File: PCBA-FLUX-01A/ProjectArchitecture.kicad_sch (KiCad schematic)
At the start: 0 parts

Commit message: Changes were made
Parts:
- added J1, J2, J3: Conn_02x06_Odd_Even, Connector_PinHeader_2.54mm:PinHeader_2x06_P2.54mm_Vertical, symbol Connector_Generic:Conn_02x06_Odd_Even
- added J4, J5, J6: Screw_Terminal_01x01, symbol Connector:Screw_Terminal_01x01
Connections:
- new net GND: J1.10 (Pin_10), J1.11 (Pin_11), J1.2 (Pin_2), J1.3 (Pin_3), J1.6 (Pin_6), J1.7 (Pin_7), J2.10 (Pin_10), J2.11 (Pin_11), J2.2 (Pin_2), J2.3 (Pin_3), J2.6 (Pin_6), J2.7 (Pin_7), J3.10 (Pin_10), J3.11 (Pin_11), J3.2 (Pin_2), J3.3 (Pin_3), J3.6 (Pin_6), J3.7 (Pin_7)
- new net Phase U/PhaseU_out: J4.1 (Pin_1)
- new net Phase U/phU_HI: J1.1 (Pin_1)
- new net Phase U/phU_LO: J1.5 (Pin_5)
- new net Phase U/phU_NTCctrl: J1.4 (Pin_4)
- new net Phase U/phU_NTCout: J1.8 (Pin_8)
- new net Phase U/phU_current: J1.9 (Pin_9)
- new net Phase U/phU_voltage: J1.12 (Pin_12)
- new net Phase V/PhaseV_out: J5.1 (Pin_1)
- new net Phase V/phV_HI: J2.1 (Pin_1)
- new net Phase V/phV_LO: J2.5 (Pin_5)
- new net Phase V/phV_NTCctrl: J2.8 (Pin_8)
- new net Phase V/phV_NTCout: J2.4 (Pin_4)
- new net Phase V/phV_current: J2.9 (Pin_9)
- new net Phase V/phV_voltage: J2.12 (Pin_12)
- new net Phase W/PhaseW_out: J6.1 (Pin_1)
- new net Phase W/phW_HI: J3.1 (Pin_1)
- new net Phase W/phW_LO: J3.5 (Pin_5)
- new net Phase W/phW_NTCctrl: J3.8 (Pin_8)
- new net Phase W/phW_NTCout: J3.4 (Pin_4)
- new net Phase W/phW_current: J3.9 (Pin_9)
- new net Phase W/phW_voltage: J3.12 (Pin_12)
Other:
- sheet Phase U ports: added PhaseU_out, phU_HI, phU_LO, phU_NTCctrl, phU_NTCout, phU_current, phU_voltage; removed none
- sheet Phase V ports: added PhaseV_out, phV_HI, phV_LO, phV_NTCctrl, phV_NTCout, phV_current, phV_voltage; removed none
- sheet Phase W ports: added PhaseW_out, phW_HI, phW_LO, phW_NTCctrl, phW_NTCout, phW_current, phW_voltage; removed none

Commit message: Finished schematic?
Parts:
- added J10, J9: Screw_Terminal_01x01, Bvrny's_library:M8_NutTerminal, symbol Connector:Screw_Terminal_01x01
- added J7, J8: Conn_02x02_Odd_Even, Connector_PinHeader_2.54mm:PinHeader_2x02_P2.54mm_Vertical, symbol Connector_Generic:Conn_02x02_Odd_Even
- J4, J5, J6: footprint (none) -> Bvrny's_library:M8_NutTerminal; now not fitted
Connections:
- net GND: now also J10.1 (Pin_1), J8.1 (Pin_1), J8.2 (Pin_2), J8.3 (Pin_3), J8.4 (Pin_4)
- new net +VSYS: J7.1 (Pin_1), J7.2 (Pin_2), J7.3 (Pin_3), J7.4 (Pin_4), J9.1 (Pin_1)
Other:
- removed sheet Power Input
- note added: "Board connectors for power to Vector"
- note added: "Board connectors to Vector"
- note added: "High current connectors"
- note added: "Inverter"
- note added: "Power input connectors"
- moved on the sheet: J1, J2, J3

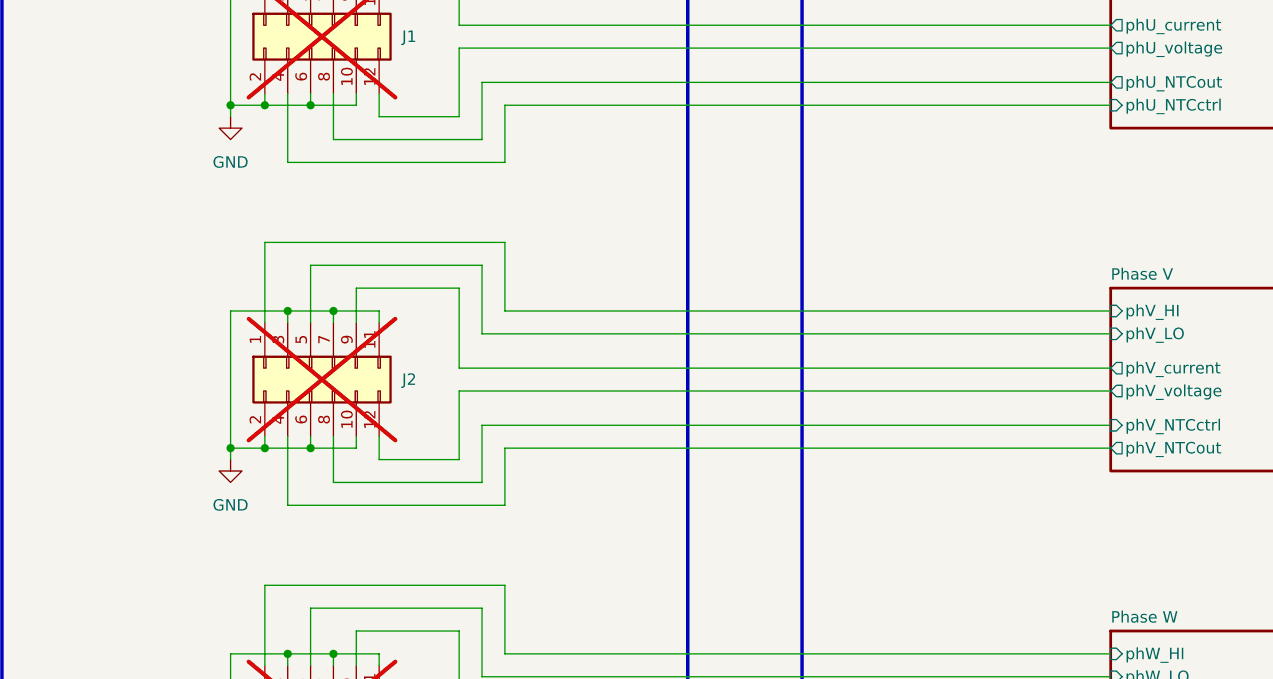
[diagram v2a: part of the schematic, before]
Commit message: Started with Flux layout
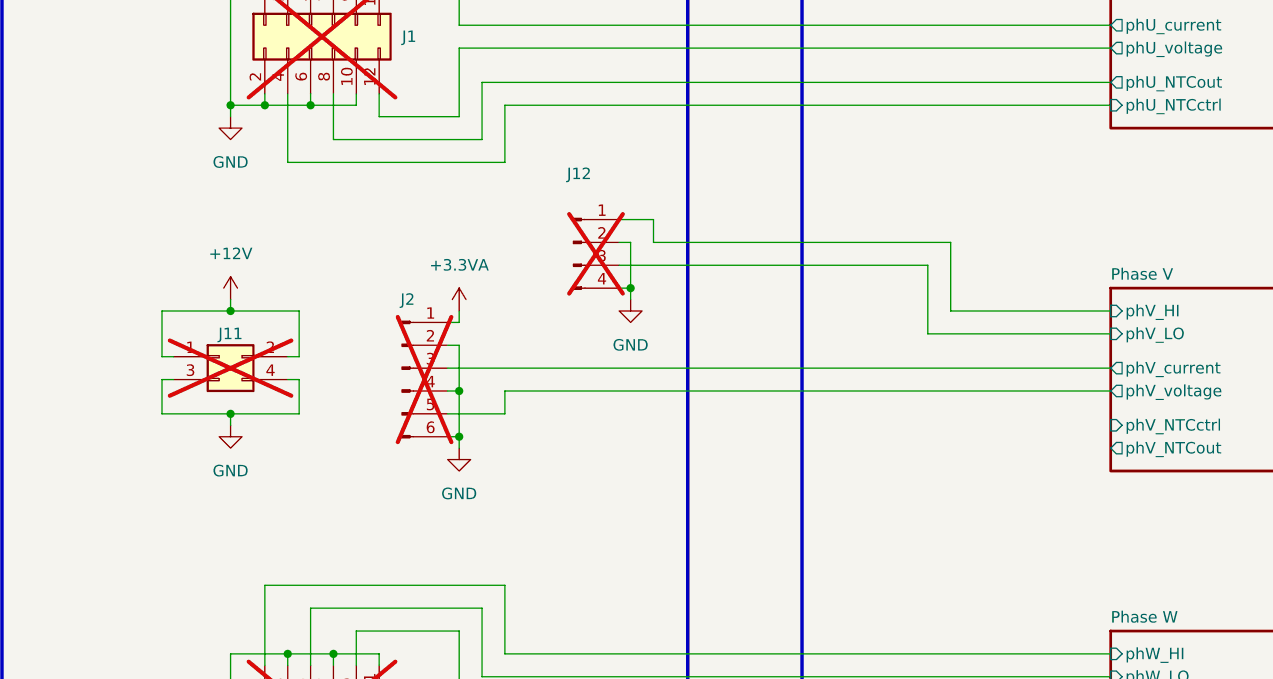
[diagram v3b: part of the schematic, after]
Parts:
- removed J2: Conn_02x06_Odd_Even, Connector_PinHeader_2.54mm:PinHeader_2x06_P2.54mm_Vertical, symbol Connector_Generic:Conn_02x06_Odd_Even
- added J11: Conn_02x02_Odd_Even, Connector_PinHeader_2.54mm:PinHeader_2x02_P2.54mm_Vertical, symbol Connector_Generic:Conn_02x02_Odd_Even
- added J12: Conn_01x04_Pin, Connector_PinHeader_2.54mm:PinHeader_1x04_P2.54mm_Vertical, symbol Connector:Conn_01x04_Pin
- added J2: Conn_01x06_Pin, Connector_PinHeader_2.54mm:PinHeader_1x06_P2.54mm_Vertical, symbol Connector:Conn_01x06_Pin
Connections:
- net GND: now also J11.3 (Pin_3), J11.4 (Pin_4), J12.2 (Pin_2), J12.4 (Pin_4), J2.2 (Pin_2), J2.4 (Pin_4), J2.6 (Pin_6)
- net Phase V/phV_HI: now also J12.1 (Pin_1)
- net Phase V/phV_LO: now also J12.3 (Pin_3)
- net Phase V/phV_current: now also J2.3 (Pin_3)
- net Phase V/phV_voltage: now also J2.5 (Pin_5)
- new net +12V: J11.1 (Pin_1), J11.2 (Pin_2)
- new net +3.3VA: J2.1 (Pin_1)

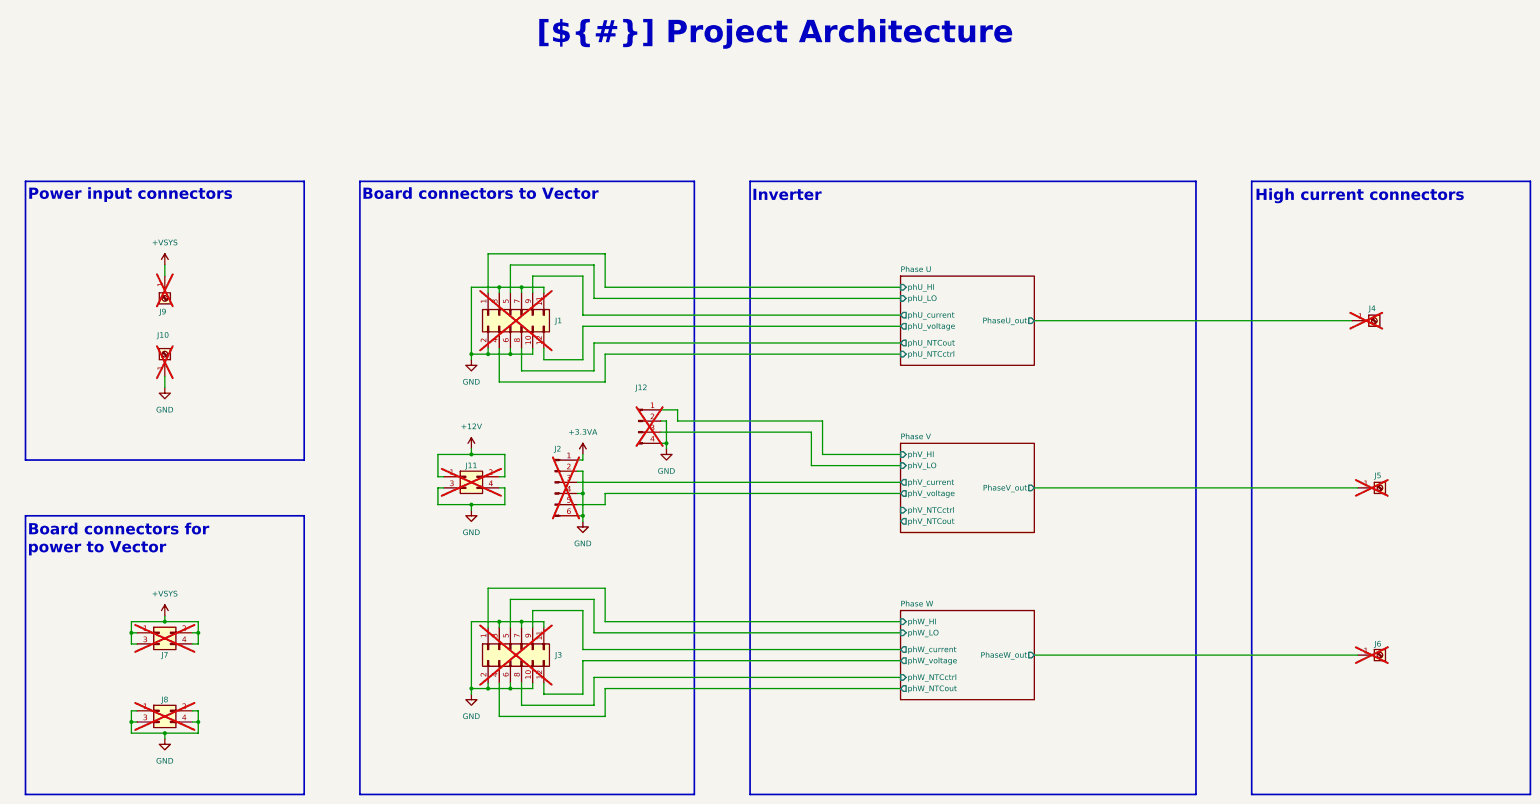
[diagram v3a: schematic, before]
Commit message: Moved the current and voltage sensing OpAmp's to Vector
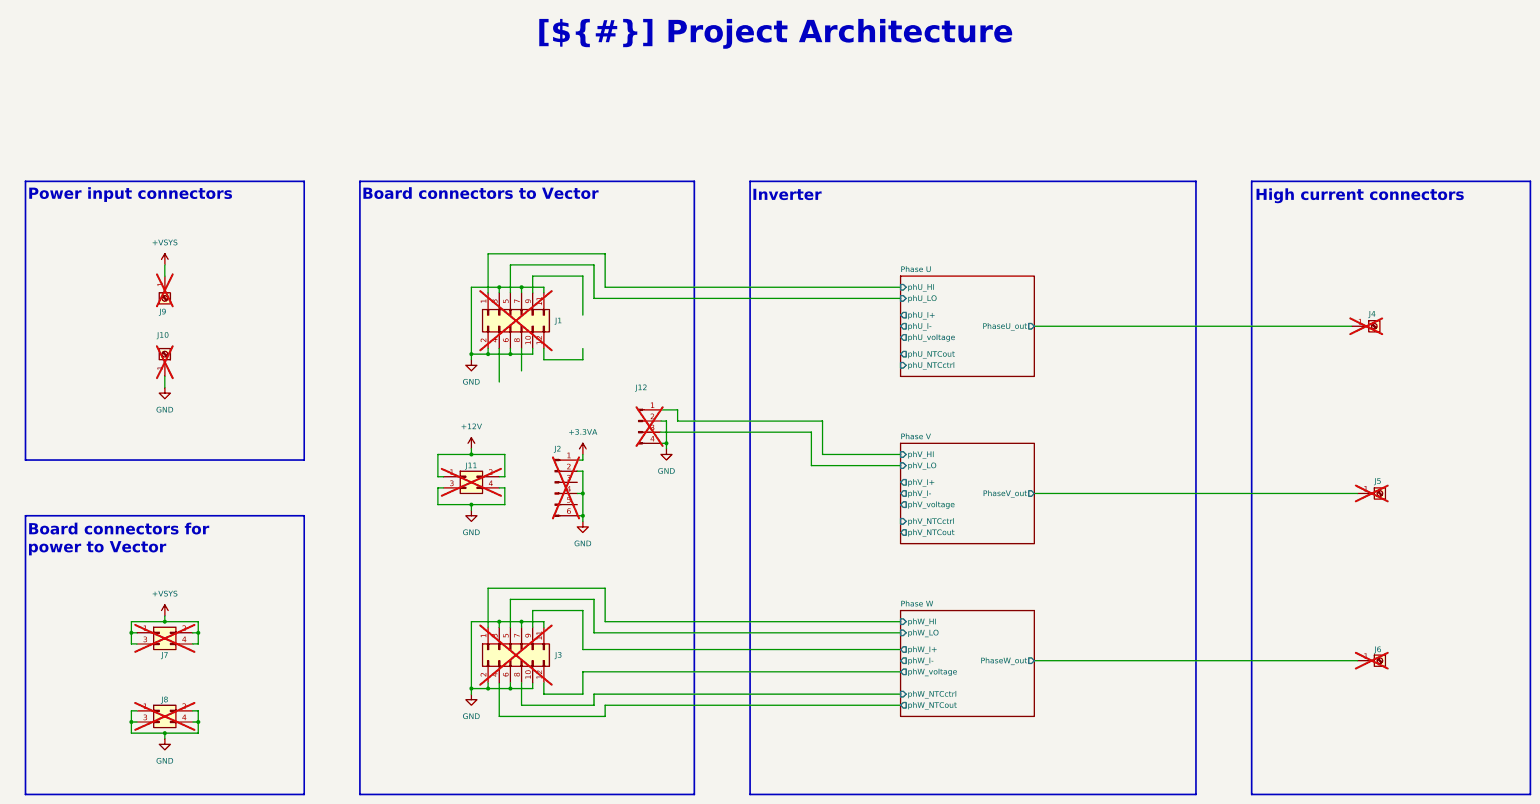
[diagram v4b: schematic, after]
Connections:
- net Phase U/phU_NTCctrl: no longer J1.4 (Pin_4)
- net Phase U/phU_NTCout: no longer J1.8 (Pin_8)
- net Phase U/phU_voltage: no longer J1.12 (Pin_12)
- net Phase V/phV_voltage: no longer J2.5 (Pin_5)
- net Phase U/phU_current: no longer names the net of J1.9 (Pin_9)
- net Phase V/phV_current: no longer names the net of J2.3 (Pin_3)
- net Phase W/phW_current renamed Phase W/phW_I+
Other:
- sheet Phase U ports: added phU_I+, phU_I-; removed phU_current
- sheet Phase V ports: added phV_I+, phV_I-; removed phV_current
- sheet Phase W ports: added phW_I+, phW_I-; removed phW_current
- moved on the sheet: J4, J5, J6
